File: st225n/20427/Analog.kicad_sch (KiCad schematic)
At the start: 119 parts, among them J1 HEADS, J4 SPINDLE, Q1 BD436, Q10 DNI, Q2 2N6039, Q3 BD436, Q4 2N6039, Q5 BD436, U13 74F08, U20 7406, U22 SSI257_2, U24 74F74, U25 74F04, U26 74LS00, U27 75448, U28 11695-502, U29 74LS123, U30 74F74, U31 74F109, U32 11642-501, U33 SSI280.2, U8 AIC-250L, U9 DP8455

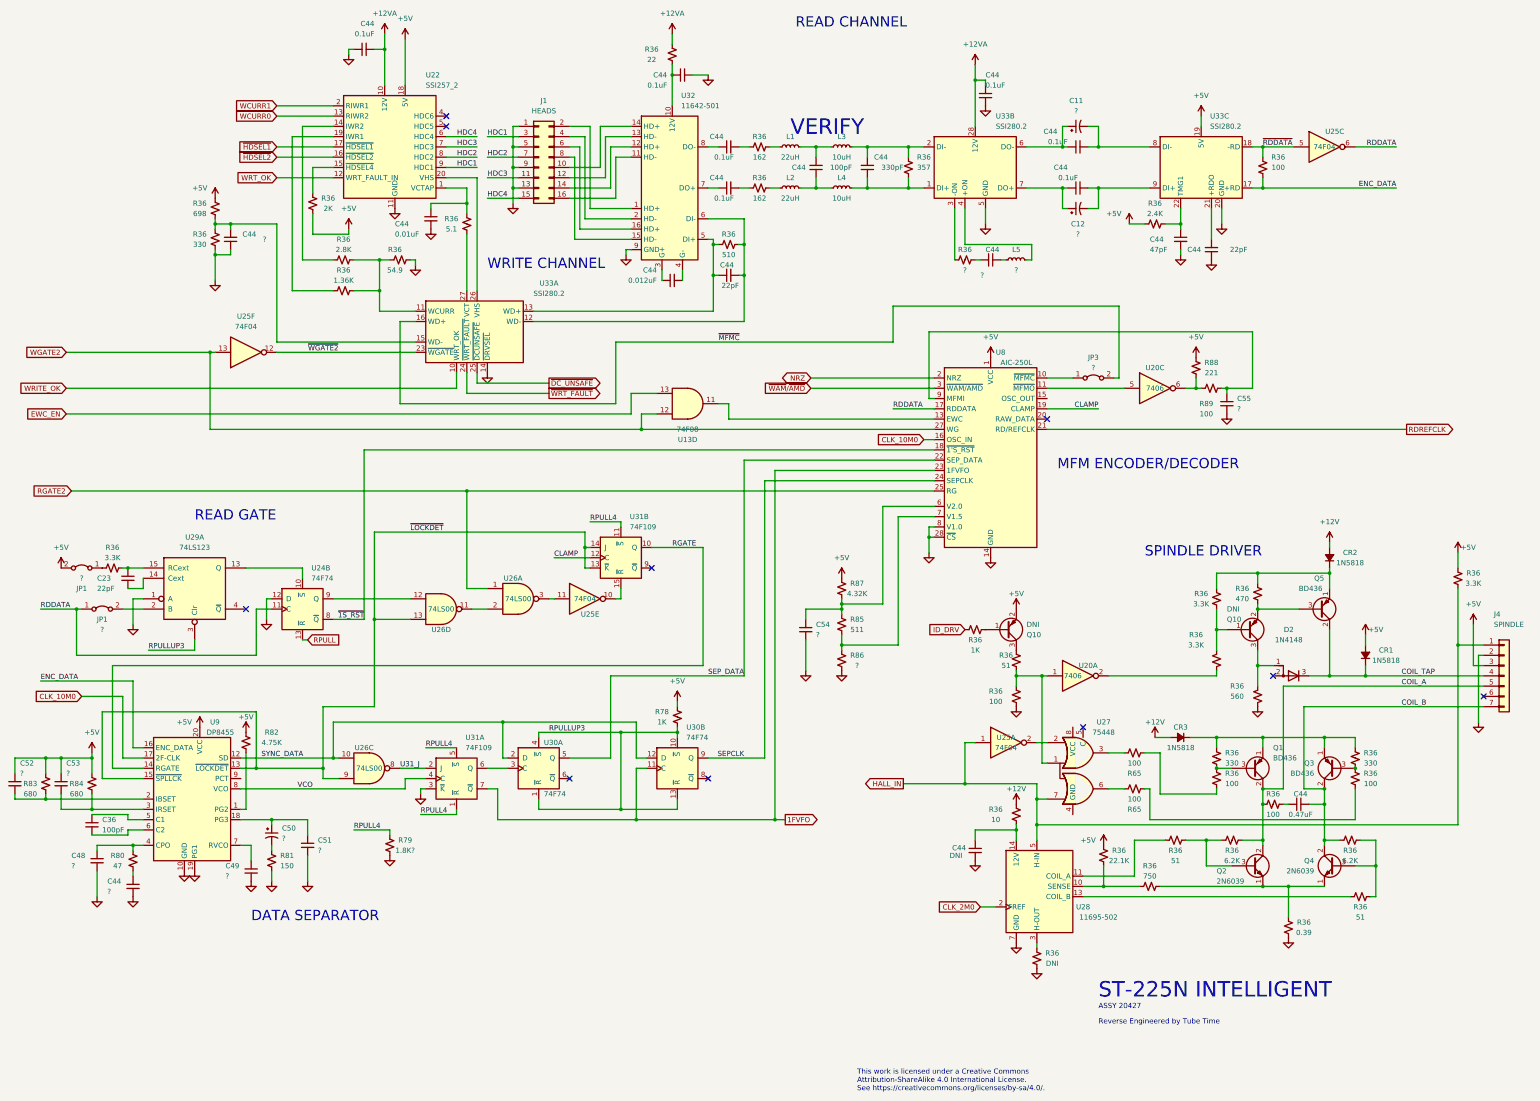
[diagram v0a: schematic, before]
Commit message: Add component values. SRAM tweak.
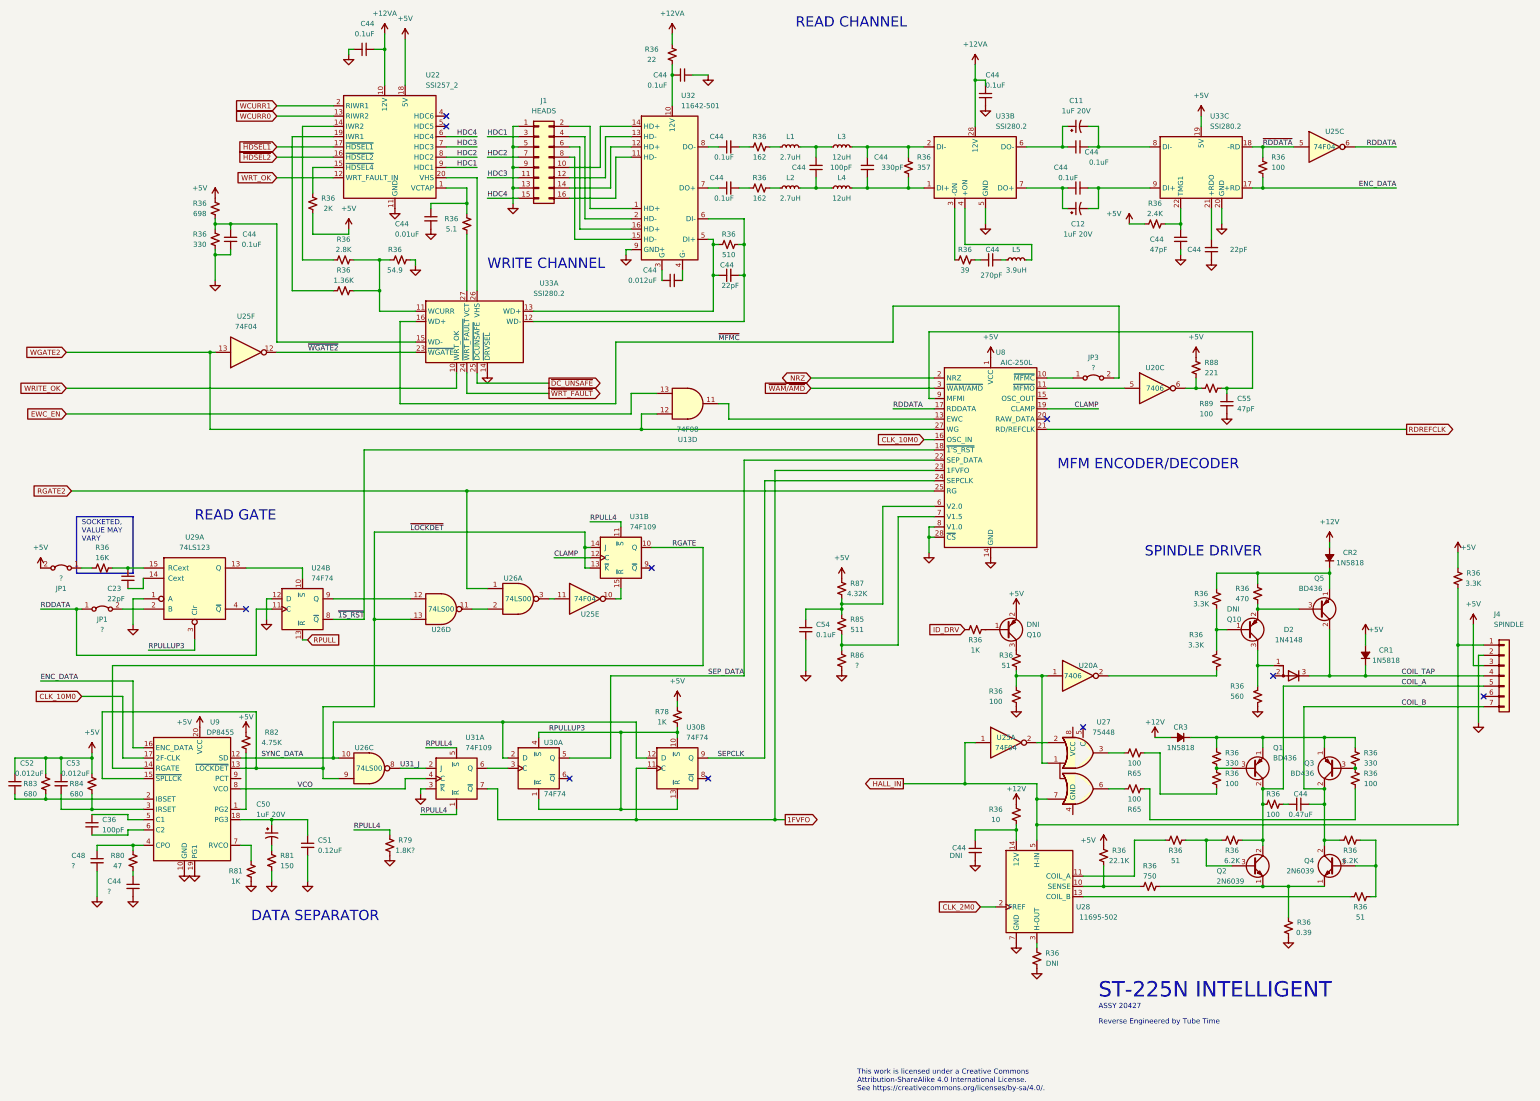
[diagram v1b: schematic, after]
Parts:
- removed C49: ?, Capacitor_SMD:C_1206_3216Metric_Pad1.33x1.80mm_HandSolder, symbol Device:C_Small
- added R81: 1K, Resistor_SMD:R_1206_3216Metric_Pad1.30x1.75mm_HandSolder, symbol Device:R_Small_US
- C11, C12, C50: value ? -> 1uF 20V
- C44, C54: value ? -> 0.1uF
- C44: value ? -> 270pF
- C51: value ? -> 0.12uF
- C52, C53: value ? -> 0.012uF
- C55: value ? -> 47pF
- L1, L2: value 22uH -> 2.7uH
- L3, L4: value 10uH -> 12uH
- L5: value ? -> 3.9uH
- R36: value ? -> 39
- R36: value 3.3K -> 16K
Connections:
- net GND: now also R81.1
- net at U9.7 (RVCO): now also R81.2
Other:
- note added: "SOCKETED, VALUE MAY VARY"
- note removed: "VERIFY"
- moved on the sheet: JP1, R36
